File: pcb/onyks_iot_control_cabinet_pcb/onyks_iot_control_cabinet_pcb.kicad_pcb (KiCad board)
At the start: 2 copper layers, 70 x 82 mm, 43 parts, among them J1 Screw_Terminal_01x02, J10 Conn_01x06_Pin, J2 Screw_Terminal_01x02, J3 Jack-DC, J4 Conn_01x03_Pin, J5 Conn_02x09_Odd_Even, J6 Conn_01x06_Socket, J7 Conn_01x02_Socket, J9 Conn_02x05_Odd_Even, Q1 NPN, Q2 NPN, Q3 PMV100ENEAR, Q5 PMV100ENEAR, SW1 SW_Push, SW2 SW_Push, SW3 SW_Push, U1 ESP32-WROOM-32D, U2 LMR51430XDDCR

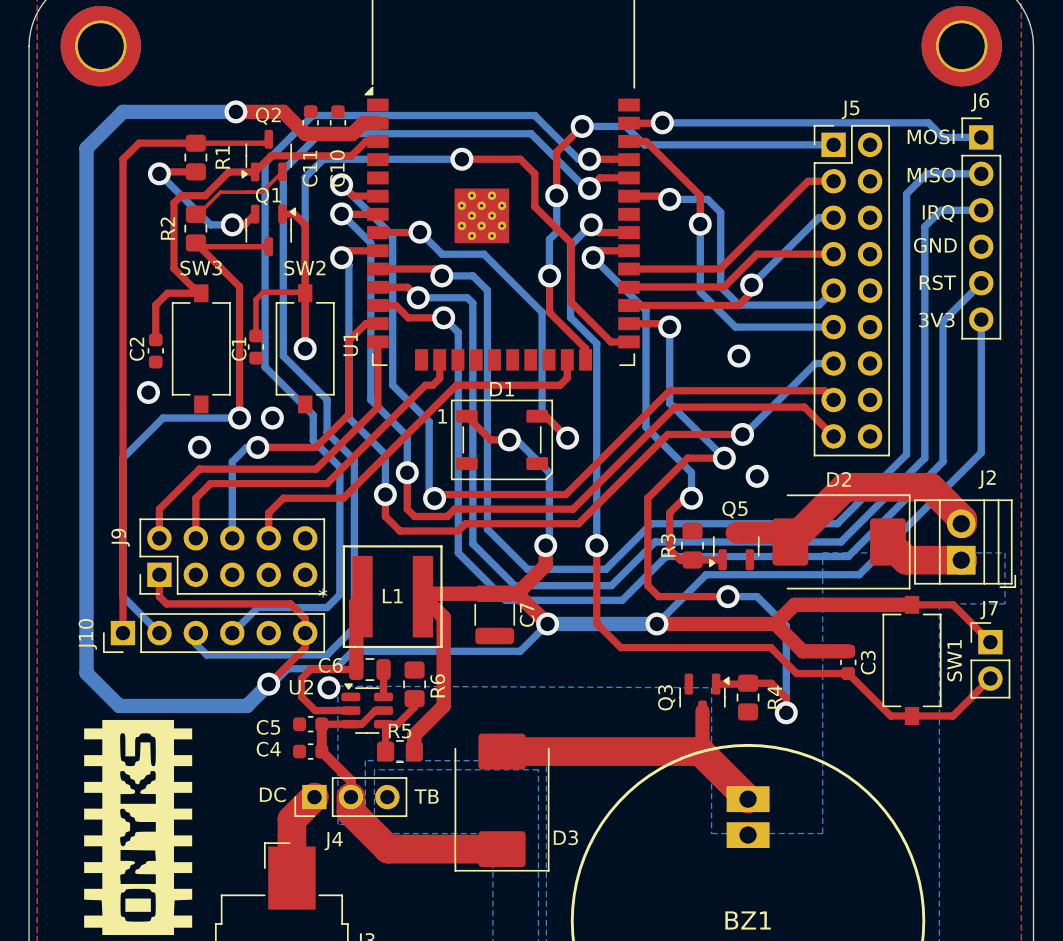
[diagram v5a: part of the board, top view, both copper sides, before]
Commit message: Silkscreen changes
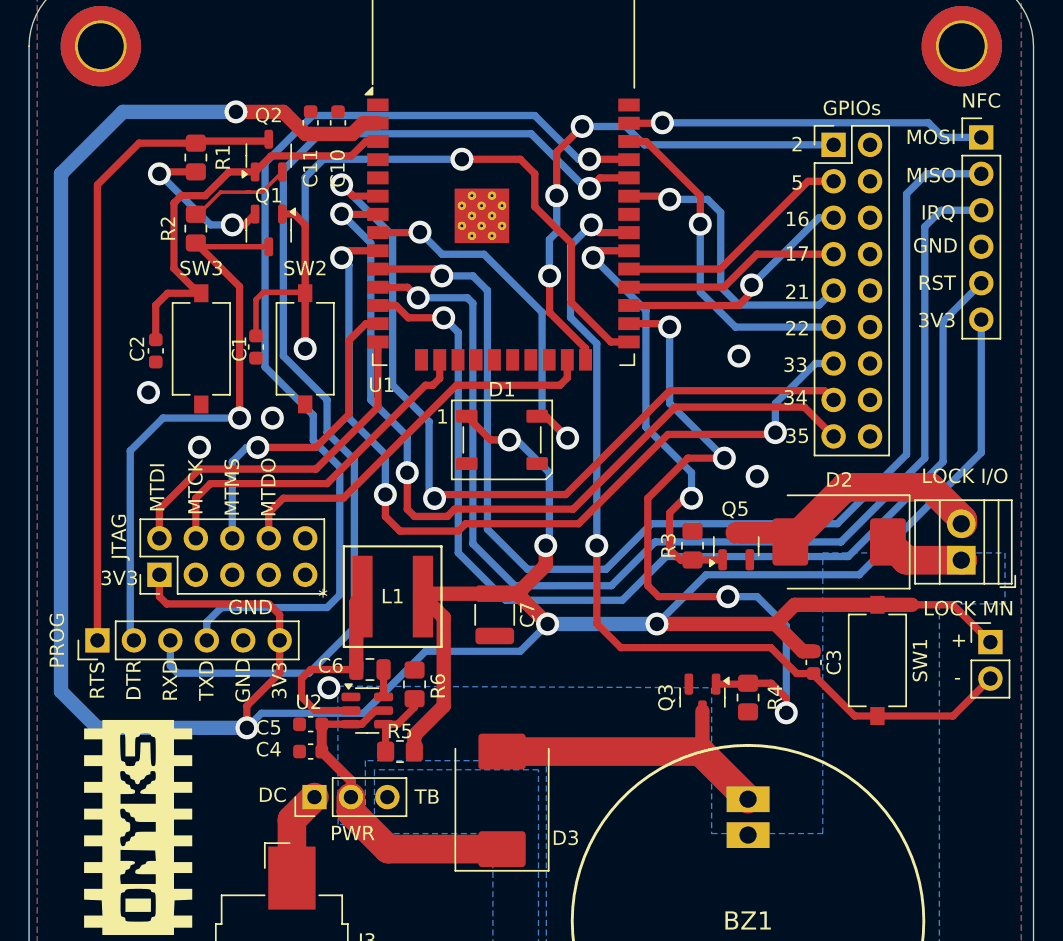
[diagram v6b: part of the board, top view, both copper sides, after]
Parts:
- LOCK I/O: renamed from J2
- LOCK MN: renamed from J7
- moved C3 2.41 mm to (209.7, 90.9)
- moved SW1 2.41 mm to (214.1, 90.8)
- moved PROG 1.85 mm to (159.8, 89.4)
- renumbered J5 to GPIOs, J9 to JTAG, J6 to NFC, J10 to PROG, J4 to PWR
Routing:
- net +3.3V: track 224.9 -> 228.4 mm
- net /MCU/RXD: track 73.9 -> 77.1 mm
- net /MCU/TXD: track 68.9 -> 71.6 mm
- net /MCU/RTS: track 43.8 -> 45.0 mm
- net /MCU/GPIO_33: track 58.5 -> 59.7 mm
- net /MCU/DTR: track 41.2 -> 40.5 mm

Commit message: PCB Review 2.0 Update
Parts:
- removed D3: S5J, Diode_SMD:D_SMC
- added C8: 47n/10V, Capacitor_SMD:C_0805_2012Metric, F.Cu at (188.5, 87.1)
- added R7: 100k, Resistor_SMD:R_0805_2012Metric_Pad1.20x1.40mm_HandSolder, F.Cu at (211.8, 93.5)
- C7: value 100u/6.3V -> 47n/10V; footprint Capacitor_SMD:C_1210_3225Metric -> Capacitor_SMD:C_0805_2012Metric
- J2: renamed from LOCK I/O
- J7: renamed from LOCK MN
- R3, R4: value 100 -> 100k
- moved C11 1.91 mm to (176.5, 53.3)
- moved C10 1.78 mm to (174.8, 53.3)
- moved C7 1.37 mm to (186.2, 87.1)
- moved SW1 1.28 mm to (215.4, 90.7)
- moved C3 1.26 mm to (209.6, 92.2), turned to 90 degrees
- renumbered PROG to J10, PWR to J4, GPIOs to J5, NFC to J6, JTAG to J9
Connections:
- C3 pad 1: +3.3V -> /MCU/GPIO_19
- C3 pad 2: /MCU/GPIO_19 -> GND
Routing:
- net Net-(BZ1--_2): track 22.4 -> 8.57 mm
- net +12V: track 29.0 -> 16.4 mm
- net /MCU/DTR: track 40.5 -> 39.0 mm
- net /MCU/GPIO_19: track 63.4 -> 64.9 mm
- net /MCU/GPIO_34: track 58.6 -> 59.9 mm
- net /MCU/GPIO_18: track 30.8 -> 31.9 mm
- net +3.3V: track 228.4 -> 227.3 mm
- net /MCU/MCU_RESET: track 29.1 -> 30.1 mm
- net Net-(Q1-B): track 11.1 -> 11.9 mm
- net /MCU/GPIO_27: track 74.4 -> 75.3 mm
- net /MCU/GPIO_35: track 58.9 -> 59.7 mm
- net /MCU/GPIO_26: track 80.8 -> 80.1 mm
- net /MCU/MTMS: track 22.5 -> 23.1 mm
- net /MCU/GPIO_32: track 26.0 -> 26.5 mm
- net GND: vias 6 -> 8

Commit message: Quick fixes
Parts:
- added R8: 240, Resistor_SMD:R_0805_2012Metric_Pad1.20x1.40mm_HandSolder, F.Cu at (220.5, 100.6)
- moved R6 0.82 mm to (212.1, 92.7), turned to -90 degrees
- moved C10 0.57 mm to (210.1, 92.5), turned to -90 degrees
- moved J2 0.51 mm to (160.3, 89.4)
- renumbered C3 to C10, C10 to C3, C11 to C4, C4 to C5, C5 to C6, C6 to C7, C7 to C8, C8 to C9, J9 to J1, J10 to J2, J1 to J3, J3 to J4, J4 to J5, J2 to J6, J5 to J8, J6 to J9, Q5 to Q3, Q3 to Q4, R5 to R3, R6 to R4, R3 to R5, R7 to R6, R4 to R7, SW2 to SW1, SW3 to SW2, SW1 to SW3
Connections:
- BZ1 pad A1: +12V -> Net-(BZ1-+_1)
- BZ1 pad B1: +12V -> Net-(BZ1-+_1)
- BZ1 pad B2: +12V -> Net-(BZ1-+_1)
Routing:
- net +12V: track 16.4 -> 79.0 mm, vias 0 -> 1
- net Net-(BZ1-+_1): track 0.00 -> 30.4 mm
- net Net-(J3-Pin_2): track 0.00 -> 25.0 mm
- net /MCU/GPIO_19: track 64.9 -> 65.9 mm
- net /MCU/RXD: track 77.1 -> 76.4 mm
- net /MCU/TXD: track 71.6 -> 71.1 mm
- net GND: vias 8 -> 6
- removed copper zone on B.Cu, net +12V
- removed copper zone on B.Cu, net Net-(J3-Pin_2)
